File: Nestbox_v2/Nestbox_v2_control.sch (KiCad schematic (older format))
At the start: 20 parts, among them P1 RX/TX, P2 TST/RST, SW1 SMD-BUTTON_2P-3.0X2.5X1.2+0.4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, U1 MSP430FR5969, Y1 Crystal

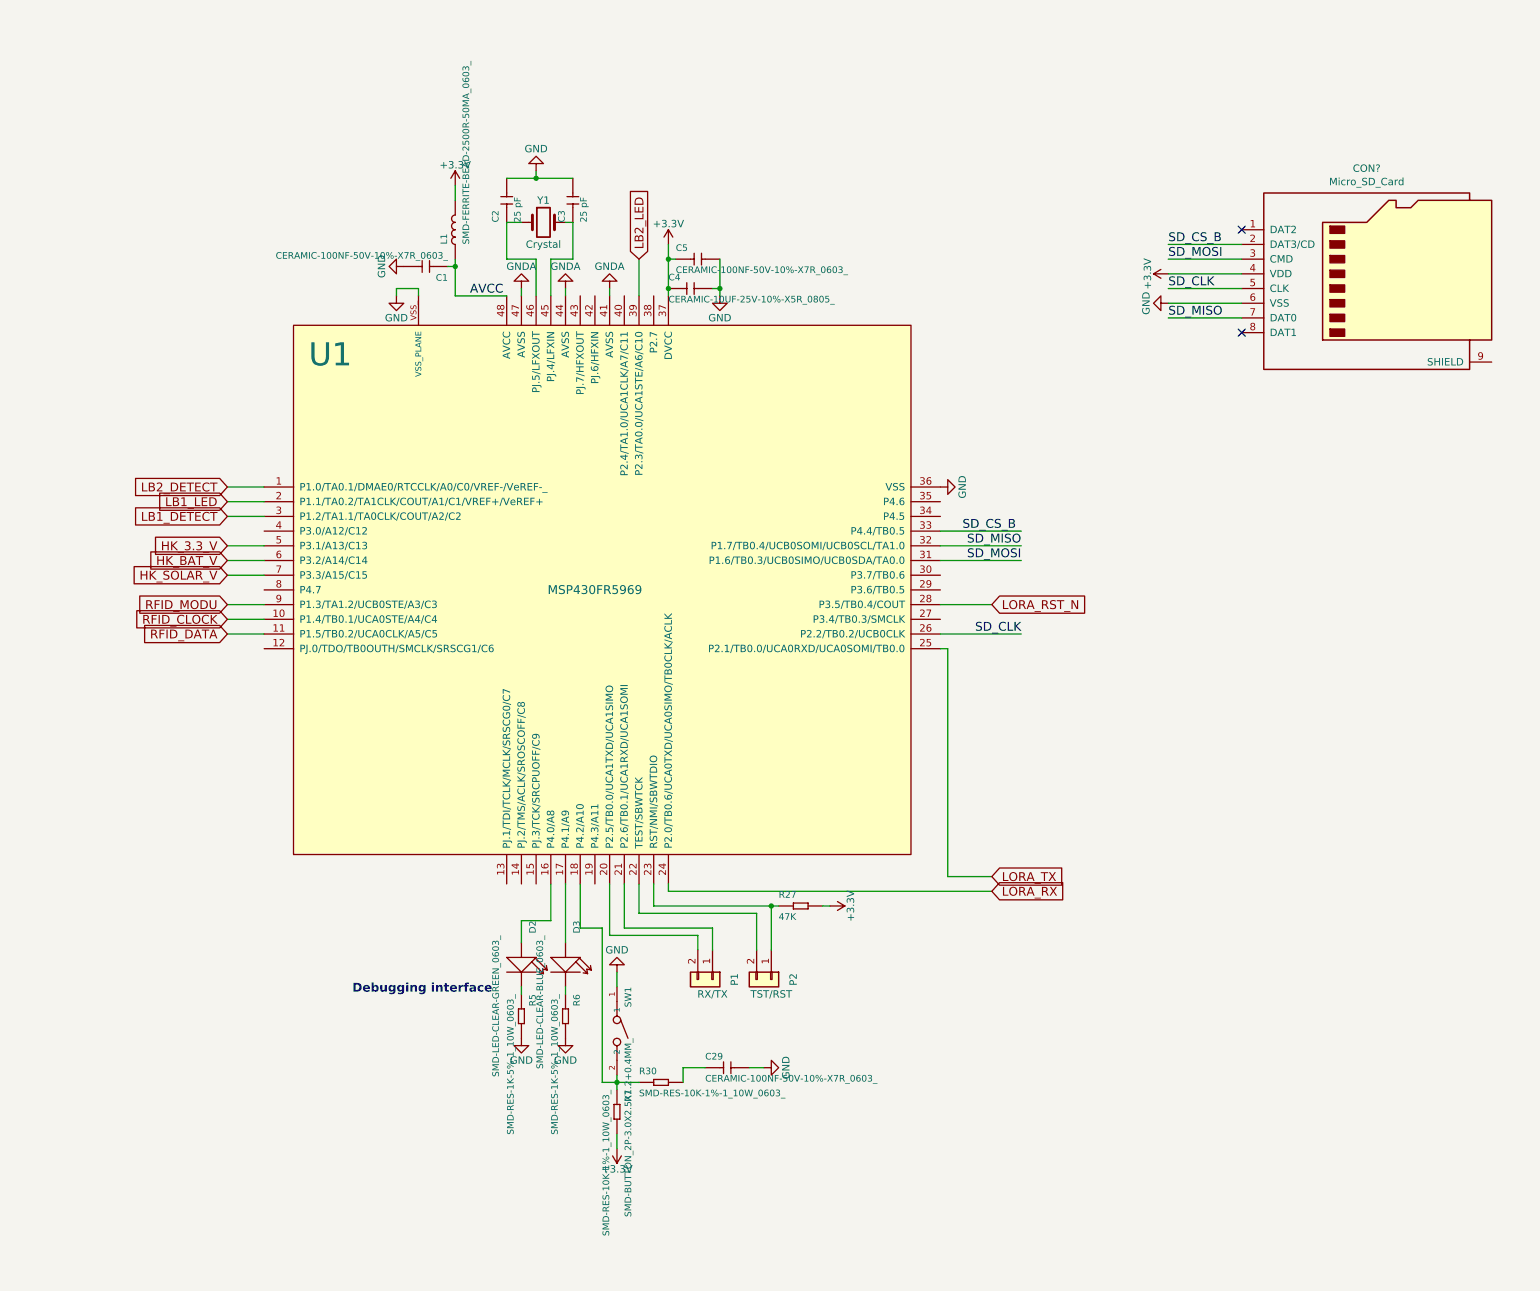
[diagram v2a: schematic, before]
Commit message: Restructures and clears of the control schematic
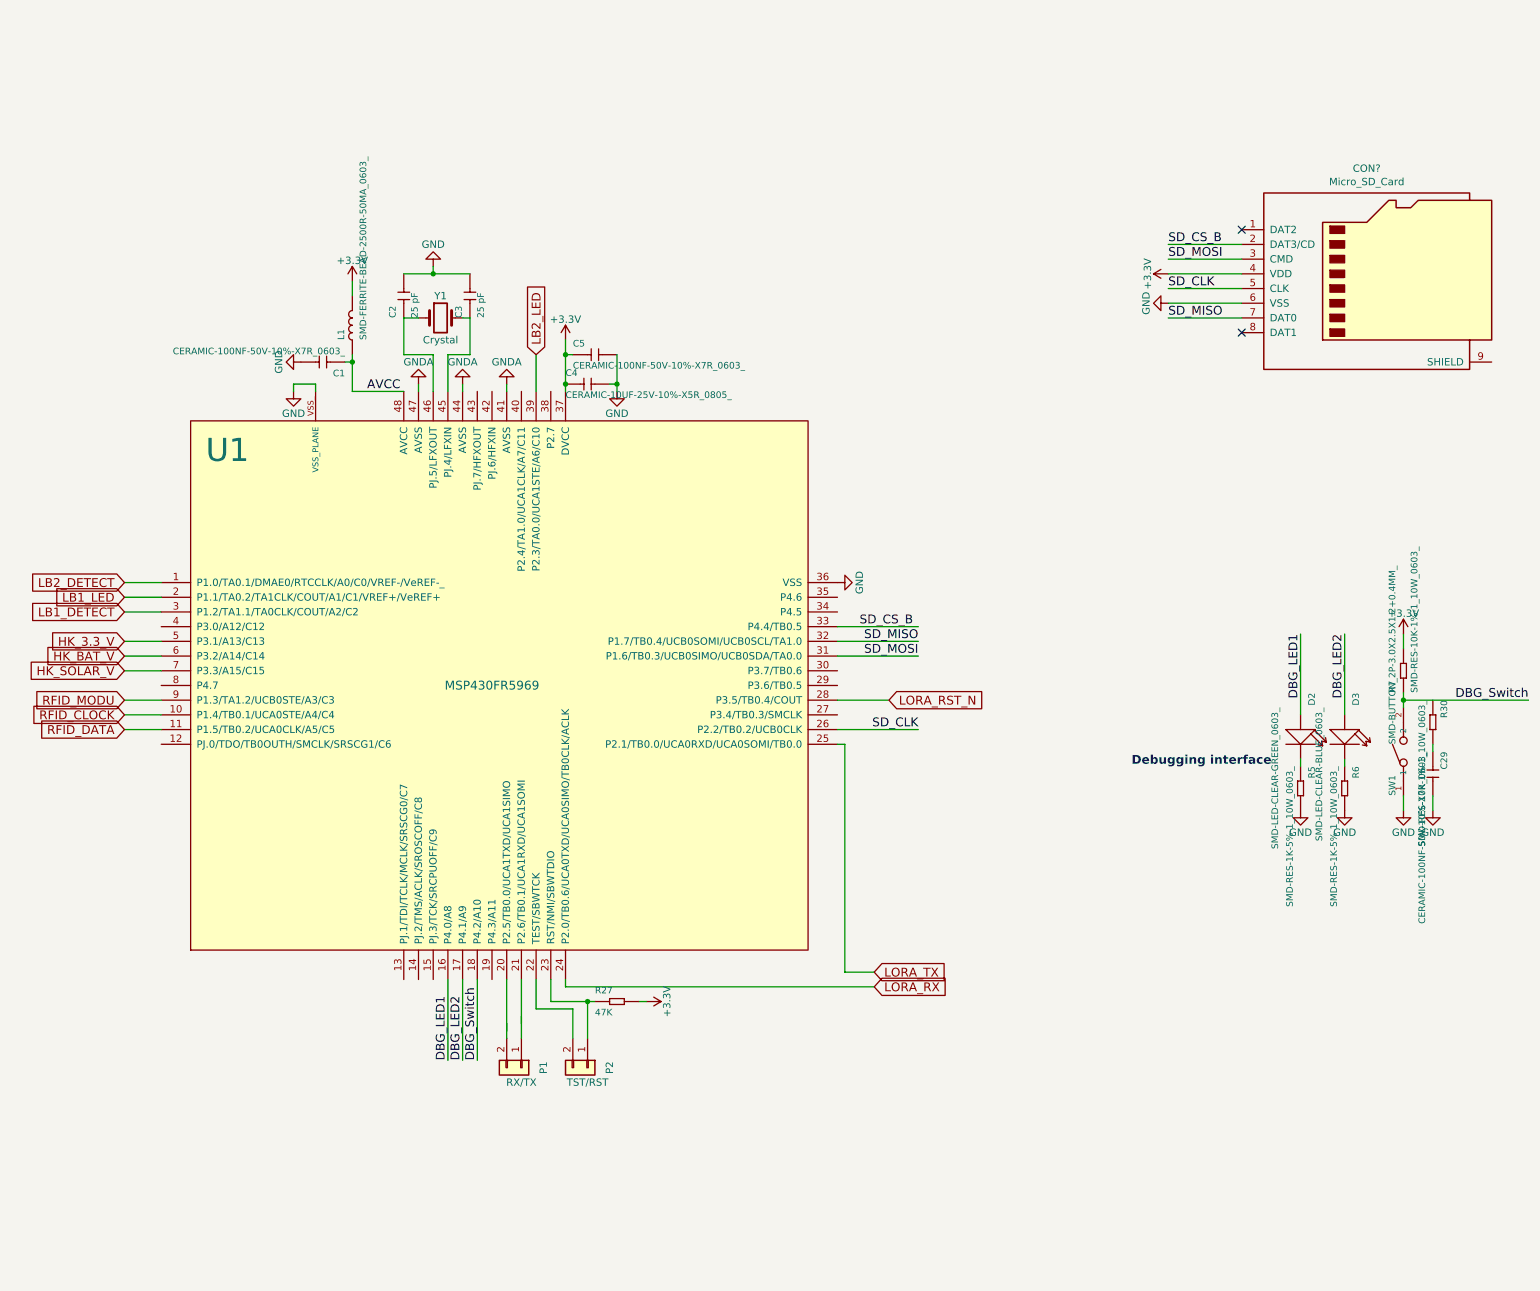
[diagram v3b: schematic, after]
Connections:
- net labels added: DBG_LED1, DBG_LED2, DBG_Switch
- wire segments 79 -> 82
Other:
- moved on the sheet: C1, C2, C29, C3, C4, C5, D2, D3, L1, P1, P2, R27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

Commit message: Connects XBee to MSP430
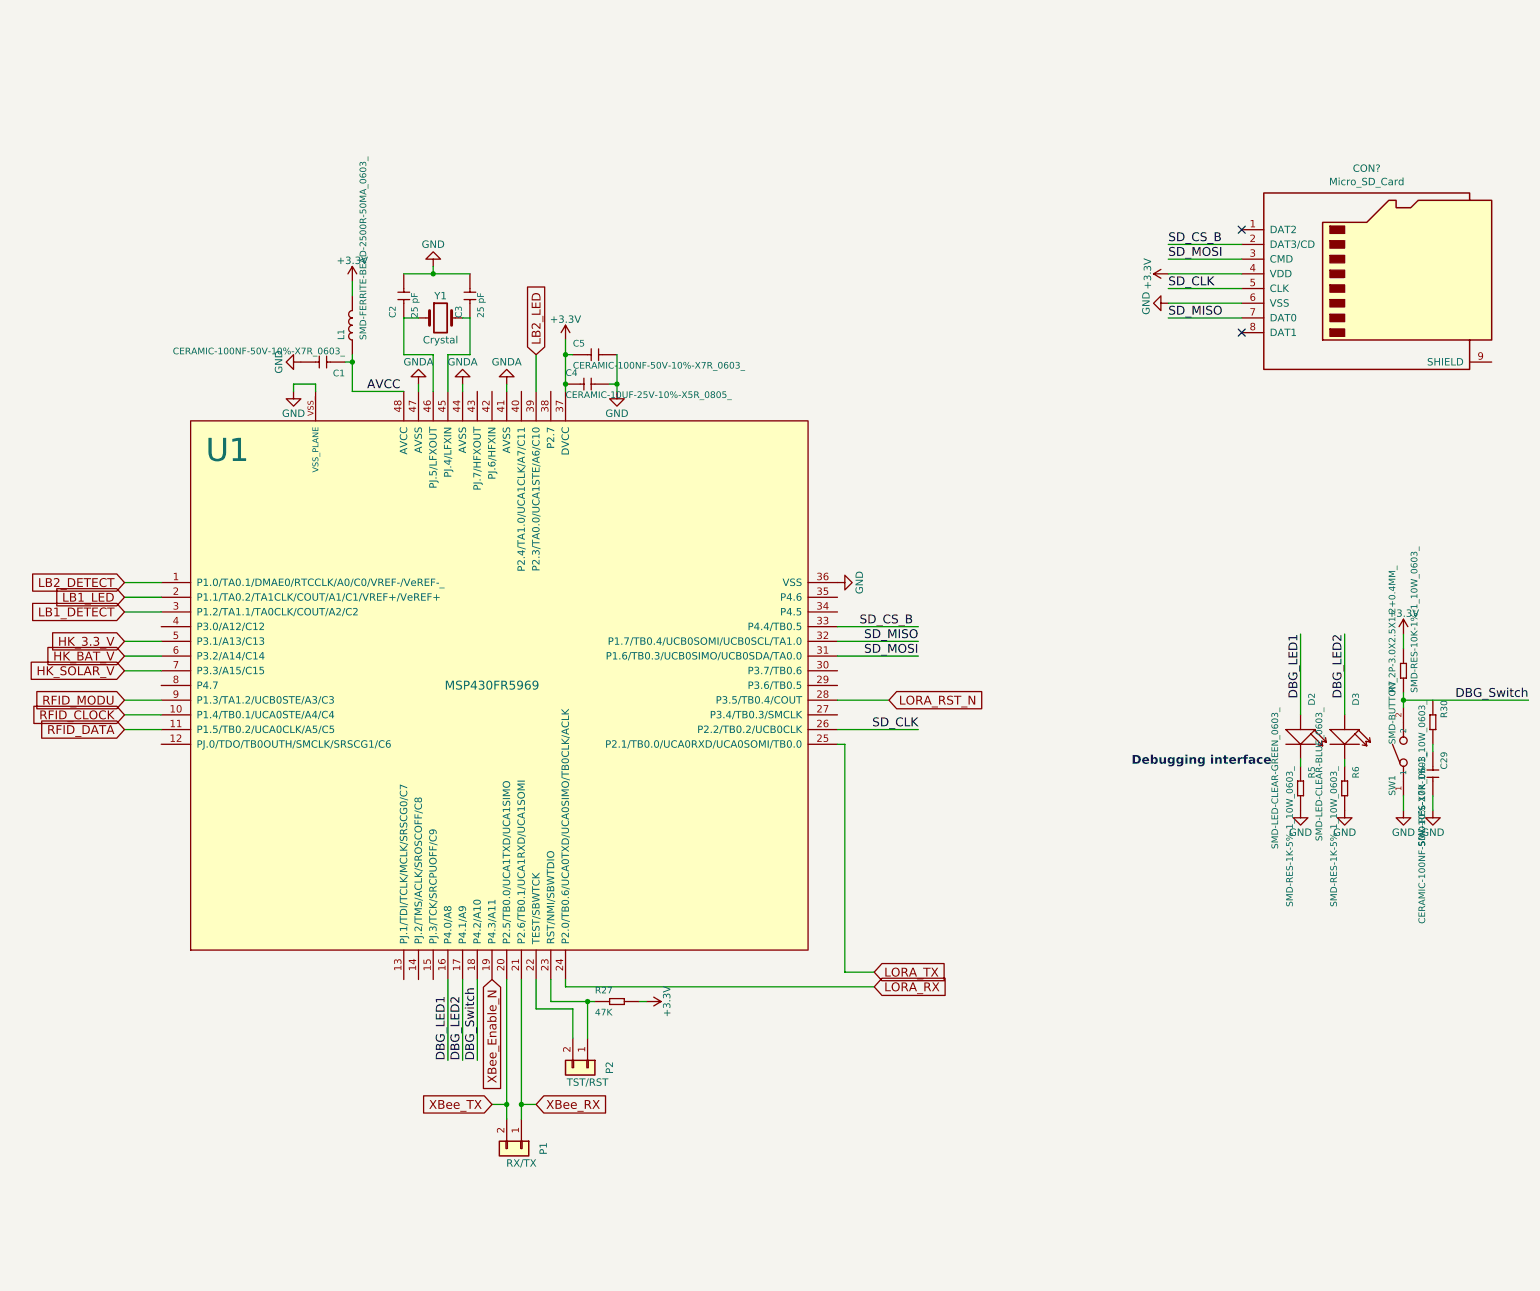
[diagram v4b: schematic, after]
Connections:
- net labels added: XBee_Enable_N, XBee_RX, XBee_TX
- wire segments 82 -> 75
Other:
- moved on the sheet: P1
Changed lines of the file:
@@
 L Conn_01x02 P1
 U 1 1 587BB574
-P 4000 7050
+P 4000 7600
 AR Path="/587BB574" Ref="P1"  Part="1"
 AR Path="/59EF7F04/587BB574" Ref="P1"  Part="1"
-F 0 "P1" H 4000 7200 50  0000 C CNN
-F 1 "RX/TX" V 4100 7050 50  0000 C CNN
-F 2 "Socket_Strips:Socket_Strip_Straight_1x02" H 4000 7050 50  0001 C CNN
-F 3 "" H 4000 7050 50  0000 C CNN
-F 4 "" H 4000 7050 50  0001 C CNN "MPN"
-F 5 "" H 4000 7050 50  0001 C CNN "SKU"
-F 6 "" H 4000 7050 50  0001 C CNN "MouserLink"
-	1    4000 7050
+F 0 "P1" H 4000 7750 50  0000 C CNN
+F 1 "RX/TX" V 4100 7600 50  0000 C CNN
+F 2 "Socket_Strips:Socket_Strip_Straight_1x02" H 4000 7600 50  0001 C CNN
+F 3 "" H 4000 7600 50  0000 C CNN
+F 4 "" H 4000 7600 50  0001 C CNN "MPN"
+F 5 "" H 4000 7600 50  0001 C CNN "SKU"
+F 6 "" H 4000 7600 50  0001 C CNN "MouserLink"
+	1    4000 7600
 	0    1    1    0
 $EndComp
@@
 AVCC
 Wire Wire Line
-	4300 2100 4300 2200
-Wire Wire Line
-	4300 2200 4300 2400
-Wire Wire Line
-	4300 2400 4300 2450
+	4300 2100 4300 2450
 Connection ~ 4300 2400
 Connection ~ 4300 2200
@@
 	2850 2450 3200 2450
 Wire Wire Line
-	2850 2200 2850 2250
-Wire Wire Line
-	2850 2250 2850 2450
+	2850 2200 2850 2450
 Wire Wire Line
 	2800 2250 2850 2250
@@
 	3400 1600 3400 1650
 Wire Wire Line
-	3200 1650 3400 1650
-Wire Wire Line
-	3400 1650 3650 1650
+	3200 1650 3650 1650
 Connection ~ 3400 1650
 Wire Wire Line
@@
 	4200 6450 4200 6600
 Wire Wire Line
-	4200 6600 4450 6600
-Wire Wire Line
-	4450 6600 4500 6600
+	4200 6600 4500 6600
 Wire Wire Line
 	4450 6600 4450 6850
 Wire Wire Line
-	10000 4600 10000 4550
-Wire Wire Line
-	10000 4550 10000 4500
+	10000 4500 10000 4600
 Wire Wire Line
 	3700 6450 3700 7000
@@
 	10000 4100 10000 4200
 Wire Wire Line
-	3900 6450 3900 6800
-Wire Wire Line
-	3900 6750 3900 6850
-Wire Wire Line
-	4000 6450 4000 6750
-Wire Wire Line
-	4000 6700 4000 6850
+	3900 6450 3900 7400
+Wire Wire Line
+	4000 6450 4000 7400
 Wire Wire Line
 	4300 6500 6400 6500
@@
 	4300 2200 4350 2200
 Wire Wire Line
-	4650 2200 4650 2400
-Wire Wire Line
-	4650 2400 4650 2450
+	4650 2200 4650 2450
 Wire Wire Line
 	4600 2400 4650 2400
@@
 	0    1    1    0
 $EndComp
+Text GLabel 3800 6450 3    60   Input ~ 0
+XBee_Enable_N
+Text GLabel 3800 7300 0    60   Input ~ 0
+XBee_TX
+Wire Wire Line
+	3800 7300 3900 7300
+Connection ~ 3900 7300
+Text GLabel 4100 7300 2    60   Input ~ 0
+XBee_RX
+Wire Wire Line
+	4100 7300 4000 7300
+Connection ~ 4000 7300
 $EndSCHEMATC

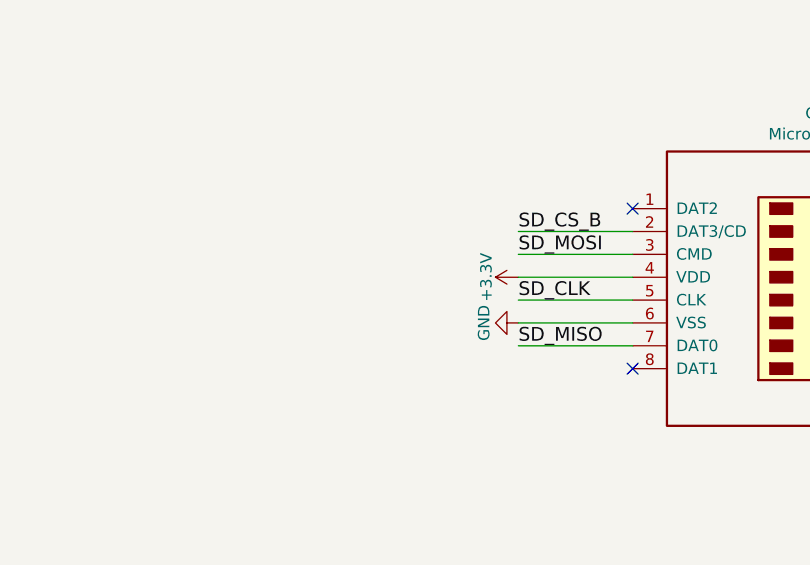
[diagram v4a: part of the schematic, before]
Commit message: Adds decoupling cap to SD Card
- 100uF and 0.1uF decoupling cap added to SD Card
- Adds 0Ohm resistor to disconnect SD Card if needed.
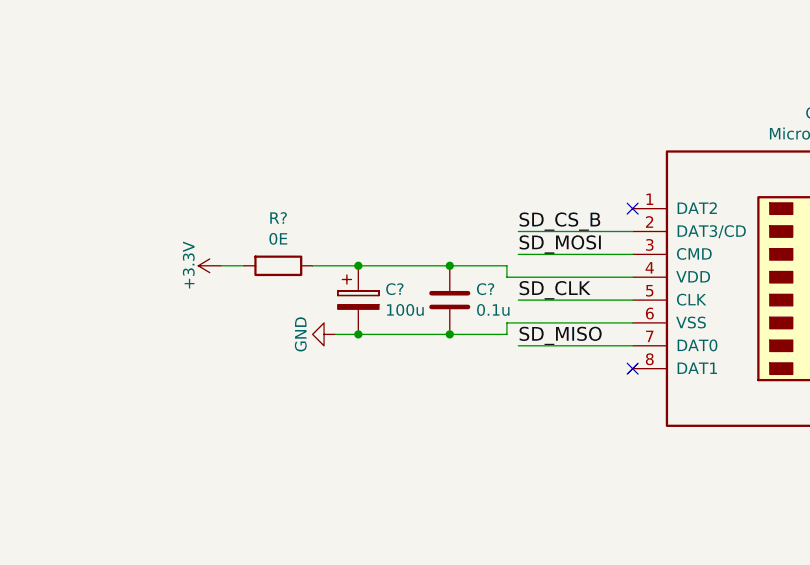
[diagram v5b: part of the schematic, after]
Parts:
- added C?: 100u, symbol CP
- added C?: 0.1u, symbol C
- added R?: 0E, symbol R
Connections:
- net +3V3: now also R?.2; no longer CON?.4 (VDD)
- net GND: now also C?.2, C?.2
- new net: C?.1, C?.1, CON?.4 (VDD), R?.1
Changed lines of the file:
@@
 	8900 1550 8400 1550
 Wire Wire Line
-	8900 1650 8400 1650
-Wire Wire Line
 	8900 1750 8400 1750
-Wire Wire Line
-	8900 1850 8400 1850
 Wire Wire Line
 	8900 1950 8400 1950
@@
 L +3.3V #PWR?
 U 1 1 59FCECA7
-P 8400 1650
-F 0 "#PWR?" H 8400 1500 50  0001 C CNN
-F 1 "+3.3V" H 8400 1790 50  0000 C CNN
-F 2 "" H 8400 1650 50  0000 C CNN
-F 3 "" H 8400 1650 50  0000 C CNN
-	1    8400 1650
+P 7100 1600
+F 0 "#PWR?" H 7100 1450 50  0001 C CNN
+F 1 "+3.3V" H 7100 1740 50  0000 C CNN
+F 2 "" H 7100 1600 50  0000 C CNN
+F 3 "" H 7100 1600 50  0000 C CNN
+	1    7100 1600
 	0    -1   -1   0
 $EndComp
@@
 L GND #PWR?
 U 1 1 59FCED84
-P 8400 1850
-F 0 "#PWR?" H 8400 1600 50  0001 C CNN
-F 1 "GND" H 8400 1700 50  0000 C CNN
-F 2 "" H 8400 1850 50  0000 C CNN
-F 3 "" H 8400 1850 50  0000 C CNN
-	1    8400 1850
+P 7600 1900
+F 0 "#PWR?" H 7600 1650 50  0001 C CNN
+F 1 "GND" H 7600 1750 50  0000 C CNN
+F 2 "" H 7600 1900 50  0000 C CNN
+F 3 "" H 7600 1900 50  0000 C CNN
+	1    7600 1900
 	0    1    1    0
 $EndComp
@@
 	4100 7300 4000 7300
 Connection ~ 4000 7300
+$Comp
+L CP C?
+U 1 1 59FF0B56
+P 7700 1750
+F 0 "C?" H 7818 1796 50  0000 L CNN
+F 1 "100u" H 7818 1705 50  0000 L CNN
+F 2 "" H 7738 1600 50  0000 C CNN
+F 3 "" H 7700 1750 50  0000 C CNN
+F 4 "667-ECE-A0JKA101" H 7700 1750 60  0001 C CNN "Mouser-Part"
+	1    7700 1750
+	1    0    0    -1
+$EndComp
+$Comp
+L C C?
+U 1 1 59FF0C21
+P 8100 1750
+F 0 "C?" H 8215 1796 50  0000 L CNN
+F 1 "0.1u" H 8215 1705 50  0000 L CNN
+F 2 "" H 8138 1600 50  0000 C CNN
+F 3 "" H 8100 1750 50  0000 C CNN
+	1    8100 1750
+	1    0    0    -1
+$EndComp
+Wire Wire Line
+	7500 1600 8350 1600
+Connection ~ 7700 1600
+Wire Wire Line
+	8350 1600 8350 1650
+Wire Wire Line
+	8350 1650 8900 1650
+Connection ~ 8100 1600
+Wire Wire Line
+	8900 1850 8350 1850
+Wire Wire Line
+	8350 1850 8350 1900
+Wire Wire Line
+	8350 1900 7600 1900
+Connection ~ 8100 1900
+Connection ~ 7700 1900
+$Comp
+L R R?
+U 1 1 59FF21A2
+P 7350 1600
+F 0 "R?" V 7143 1600 50  0000 C CNN
+F 1 "0E" V 7234 1600 50  0000 C CNN
+F 2 "" V 7280 1600 50  0000 C CNN
+F 3 "" H 7350 1600 50  0000 C CNN
+	1    7350 1600
+	0    1    1    0
+$EndComp
+Wire Wire Line
+	7100 1600 7200 1600
 $EndSCHEMATC

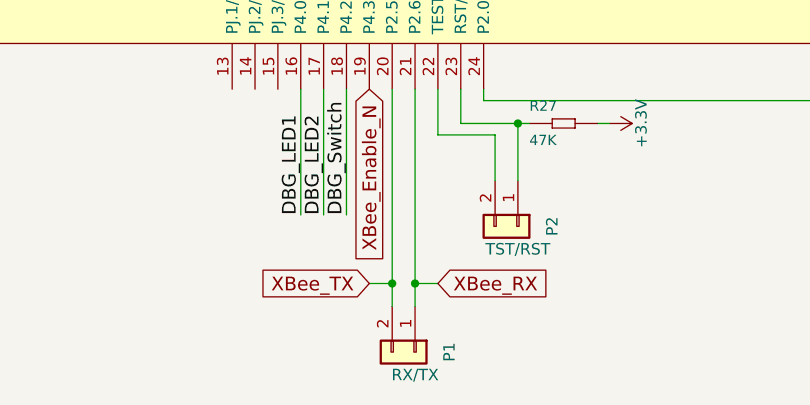
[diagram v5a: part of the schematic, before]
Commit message: Adds ESP-12S to communication schematics
- The ESP-12S was added to the communication schematics, as an alternative to
the XBee controller.
- XBee_TX and RX signals were renamed to DATA_TX and RX
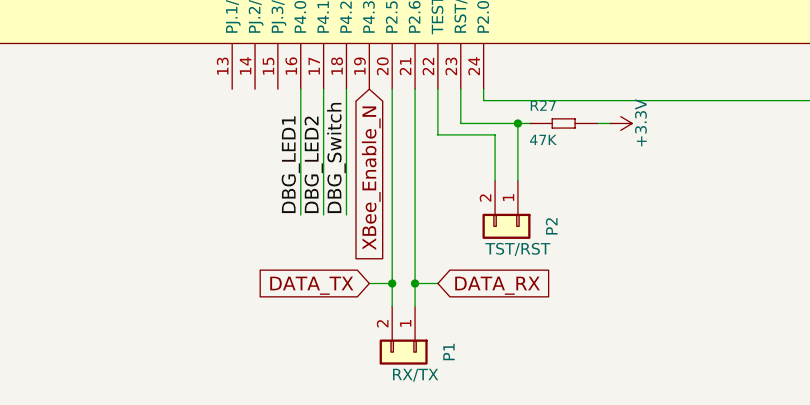
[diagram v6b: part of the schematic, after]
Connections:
- net XBee_RX renamed DATA_RX
- net XBee_TX renamed DATA_TX
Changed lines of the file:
@@
 XBee_Enable_N
 Text GLabel 3800 7300 0    60   Input ~ 0
-XBee_TX
+DATA_TX
 Wire Wire Line
 	3800 7300 3900 7300
 Connection ~ 3900 7300
 Text GLabel 4100 7300 2    60   Input ~ 0
-XBee_RX
+DATA_RX
 Wire Wire Line
 	4100 7300 4000 7300
